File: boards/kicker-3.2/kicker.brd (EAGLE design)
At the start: 141 x 146.1 mm, 160 parts, among them J1 B2PS-VH(LF)(SN), J2 HFW8R-1ST, J3 B2PS-VH(LF)(SN), J4 B2PS-VH(LF)(SN), J5 2-PIN_2MM-H, J6 3-PIN_2MM-H, J7 !BTN_KCK_PRE_EXT, J8 !BTN_CHP_PRE_EXT, J9 !BTN_CHG_PRE_EXT, Q1 ATP302ATPAK, Q10 BSS806NSOT-23-3, Q2 IRFS4227, Q3 BSS127, Q4 BSS127, Q5 BSS127, Q6 BSS127, Q7 AOD1N60, T1 DA203X-ALDA2034, U1 MPM3620GQV-P, U2 15V, U3 LT3751FE, U4 AT32ATQFP44, U5 IX4427N, U6 MAX6817, U7 MAX6817

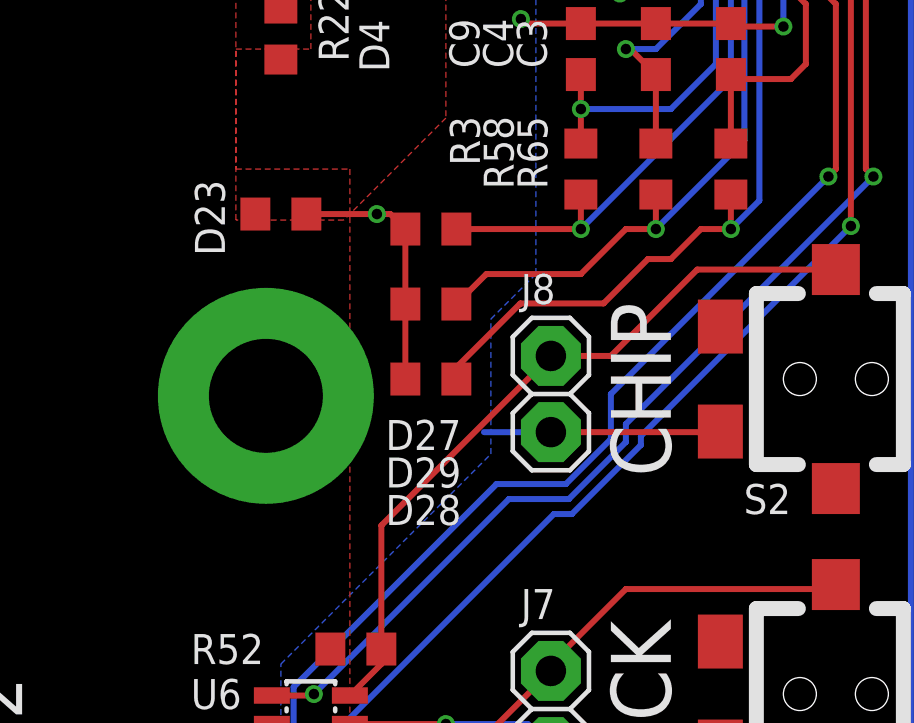
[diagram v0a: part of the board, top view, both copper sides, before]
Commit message: remove unnecessary TVS diodes clapming DIO rails
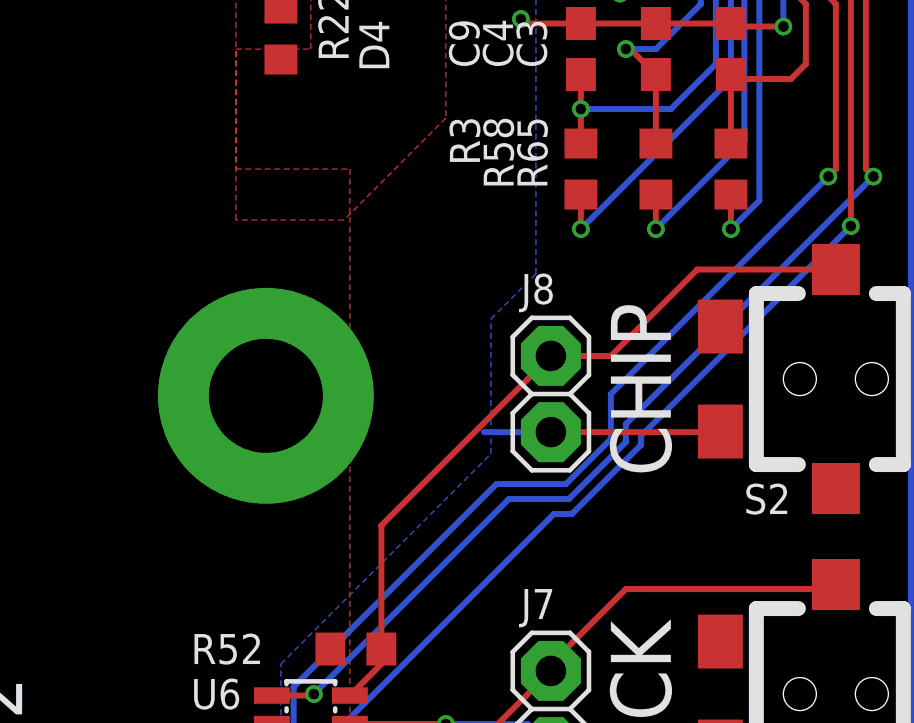
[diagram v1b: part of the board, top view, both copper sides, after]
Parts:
- removed D23, D27, D28, D29: PESD5V0C1USFYL, RoboJackets-Diodes:R0603
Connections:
- net !DONE!_RAW: no longer D29.2
- net !FAULT!_RAW: no longer D28.2
- net +5V: no longer D23.2
- net CHARGE_RAW: no longer D27.2
- net GND: no longer D23.1, D27.1, D28.1, D29.1
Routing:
- net !FAULT!_RAW: track 316.2 -> 304.7 mm
- net GND: track 355.0 -> 346.5 mm, vias 355 -> 354
- net !DONE!_RAW: track 304.3 -> 296.6 mm
- net CHARGE_RAW: track 292.3 -> 288.2 mm
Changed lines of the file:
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@@
 <attribute name="VALUE" x="-51.465" y="-16.295" size="1.27" layer="27" rot="R180"/>
-</element>
-<element name="D23" library="RoboJackets-Diodes" package="R0603" package3d_urn="urn:adsk.eagle:package:23555/3" value="PESD5V0C1USFYL" x="49" y="7" smashed="yes" rot="R180">
-<attribute name="NAME" x="46.135" y="8.135" size="1" layer="25" rot="R270"/>
-<attribute name="VALUE" x="49.635" y="8.905" size="1.27" layer="27" rot="R180"/>
 </element>
 <element name="D5" library="RoboJackets-LEDs" package="CHIP-LED0603" value="YELLOW" x="32.5" y="74.5" smashed="yes" rot="R180">
@@
 <attribute name="NAME" x="55.615" y="11.865" size="1" layer="25" font="vector" rot="R90"/>
 <attribute name="VALUE" x="60.905" y="11.865" size="1.27" layer="27" rot="R90"/>
-</element>
-<element name="D27" library="RoboJackets-Diodes" package="R0603" package3d_urn="urn:adsk.eagle:package:23555/3" value="PESD5V0C1USFYL" x="54" y="6.5" smashed="yes">
-<attribute name="NAME" x="52.49" y="-0.865" size="1" layer="25" font="vector"/>
-<attribute name="VALUE" x="53.365" y="4.595" size="1.27" layer="27"/>
-</element>
-<element name="D28" library="RoboJackets-Diodes" package="R0603" package3d_urn="urn:adsk.eagle:package:23555/3" value="PESD5V0C1USFYL" x="54" y="1.5" smashed="yes">
-<attribute name="NAME" x="52.49" y="-3.365" size="1" layer="25" font="vector"/>
-<attribute name="VALUE" x="53.365" y="-0.405" size="1.27" layer="27"/>
-</element>
-<element name="D29" library="RoboJackets-Diodes" package="R0603" package3d_urn="urn:adsk.eagle:package:23555/3" value="PESD5V0C1USFYL" x="54" y="4" smashed="yes">
-<attribute name="NAME" x="52.49" y="-2.115" size="1" layer="25" font="vector"/>
-<attribute name="VALUE" x="53.365" y="2.095" size="1.27" layer="27"/>
 </element>
 <element name="R4" library="rcl" package="R0603" value="100k" x="41" y="65.5" smashed="yes" rot="MR180">
@@
 <contactref element="U4" pad="28"/>
 <contactref element="U4" pad="39"/>
-<contactref element="D23" pad="1"/>
 <contactref element="C9" pad="2"/>
 <contactref element="R4" pad="1"/>
-<contactref element="D27" pad="1"/>
-<contactref element="D28" pad="1"/>
 <contactref element="C3" pad="2"/>
 <contactref element="C4" pad="2"/>
-<contactref element="D29" pad="1"/>
 <contactref element="C11" pad="-"/>
 <contactref element="C29" pad="2"/>
@@
 <wire x1="57.15" y1="13.35" x2="57" y2="13.5" width="0.2" layer="1"/>
 <via x="57" y="13.5" extent="1-16" drill="0.35"/>
-<wire x1="49.85" y1="7" x2="52.2" y2="7" width="0.2" layer="1"/>
-<via x="52.2" y="7" extent="1-16" drill="0.35"/>
-<wire x1="52.65" y1="7" x2="53.15" y2="6.5" width="0.2" layer="1"/>
-<wire x1="52.65" y1="7" x2="52.2" y2="7" width="0.2" layer="1"/>
-<wire x1="53.15" y1="6.5" x2="53.15" y2="4" width="0.2" layer="1"/>
-<wire x1="53.15" y1="4" x2="53.15" y2="1.5" width="0.2" layer="1"/>
 <via x="-37.25" y="1" extent="1-16" drill="0.35"/>
 <contactref element="D24" pad="A"/>
@@
 <wire x1="34.5" y1="71" x2="34.5" y2="69.5" width="0.1524" layer="1"/>
 <contactref element="C2" pad="1"/>
-<contactref element="D23" pad="2"/>
 <wire x1="47.45" y1="58.05" x2="47.45" y2="57.022878125" width="0.2" layer="1"/>
 <wire x1="34.5" y1="71" x2="47.45" y2="58.05" width="0.2" layer="1"/>
@@
 <contactref element="R3" pad="2"/>
 <contactref element="R4" pad="2"/>
-<contactref element="D27" pad="2"/>
 <wire x1="-69.1" y1="46.3" x2="-69.1" y2="-11.55" width="0.2" layer="16"/>
 <wire x1="-69.1" y1="46.3" x2="-63.475" y2="51.925" width="0.2" layer="16"/>
@@
 <wire x1="64" y1="27.025" x2="64" y2="11.5" width="0.2" layer="16"/>
 <wire x1="45.6" y1="65.5" x2="41.85" y2="65.5" width="0.2" layer="16"/>
-<wire x1="59" y1="6.5" x2="54.85" y2="6.5" width="0.2" layer="1"/>
 <wire x1="-7.2" y1="75.9" x2="-6.3556" y2="75.9" width="0.2" layer="16"/>
 <wire x1="-6.3556" y1="75.9" x2="-6.3506" y2="75.895" width="0.2" layer="16"/>
@@
 <contactref element="R19" pad="1"/>
 <contactref element="R58" pad="2"/>
-<contactref element="D29" pad="2"/>
 <wire x1="39.725" y1="67.75" x2="41.625" y2="67.75" width="0.2" layer="16"/>
 <via x="41.625" y="67.75" extent="1-16" drill="0.35"/>
@@
 <wire x1="46.375" y1="63" x2="46.5" y2="63" width="0.2" layer="1"/>
 <wire x1="46.375" y1="63" x2="41.625" y2="67.75" width="0.2" layer="1"/>
-<wire x1="61.5" y1="6.5" x2="60.5" y2="6.5" width="0.2" layer="1"/>
-<wire x1="60.5" y1="6.5" x2="59" y2="5" width="0.2" layer="1"/>
-<wire x1="59" y1="5" x2="55.85" y2="5" width="0.2" layer="1"/>
-<wire x1="55.85" y1="5" x2="54.85" y2="4" width="0.2" layer="1"/>
 <via x="-6" y="76.5" extent="1-16" drill="0.35"/>
 <wire x1="-7.175" y1="76.5" x2="-6" y2="76.5" width="0.2" layer="16"/>
@@
 <contactref element="U3" pad="6"/>
 <contactref element="R65" pad="2"/>
-<contactref element="D28" pad="2"/>
 <contactref element="R57" pad="1"/>
 <contactref element="Q4" pad="1"/>
@@
 <wire x1="41.5" y1="70" x2="47.5" y2="64" width="0.2" layer="1"/>
 <via x="47.5" y="64" extent="1-16" drill="0.35"/>
-<wire x1="64" y1="6.5" x2="63" y2="6.5" width="0.2" layer="1"/>
-<wire x1="63" y1="6.5" x2="62" y2="5.5" width="0.2" layer="1"/>
-<wire x1="62" y1="5.5" x2="61.235025" y2="5.5" width="0.2" layer="1"/>
-<wire x1="61.235025" y1="5.5" x2="59.755025" y2="4.02" width="0.2" layer="1"/>
-<wire x1="59.755025" y1="4.02" x2="56.98223125" y2="4.02" width="0.2" layer="1"/>
-<wire x1="56.98223125" y1="4.02" x2="54.85" y2="1.88776875" width="0.2" layer="1"/>
-<wire x1="54.85" y1="1.5" x2="54.85" y2="1.88776875" width="0.2" layer="1"/>
 <wire x1="-52.895" y1="62.605" x2="-52.895" y2="55.22249375" width="0.2" layer="16"/>
 <wire x1="-52.895" y1="55.22249375" x2="-55.26629375" y2="52.8512" width="0.2" layer="16"/>

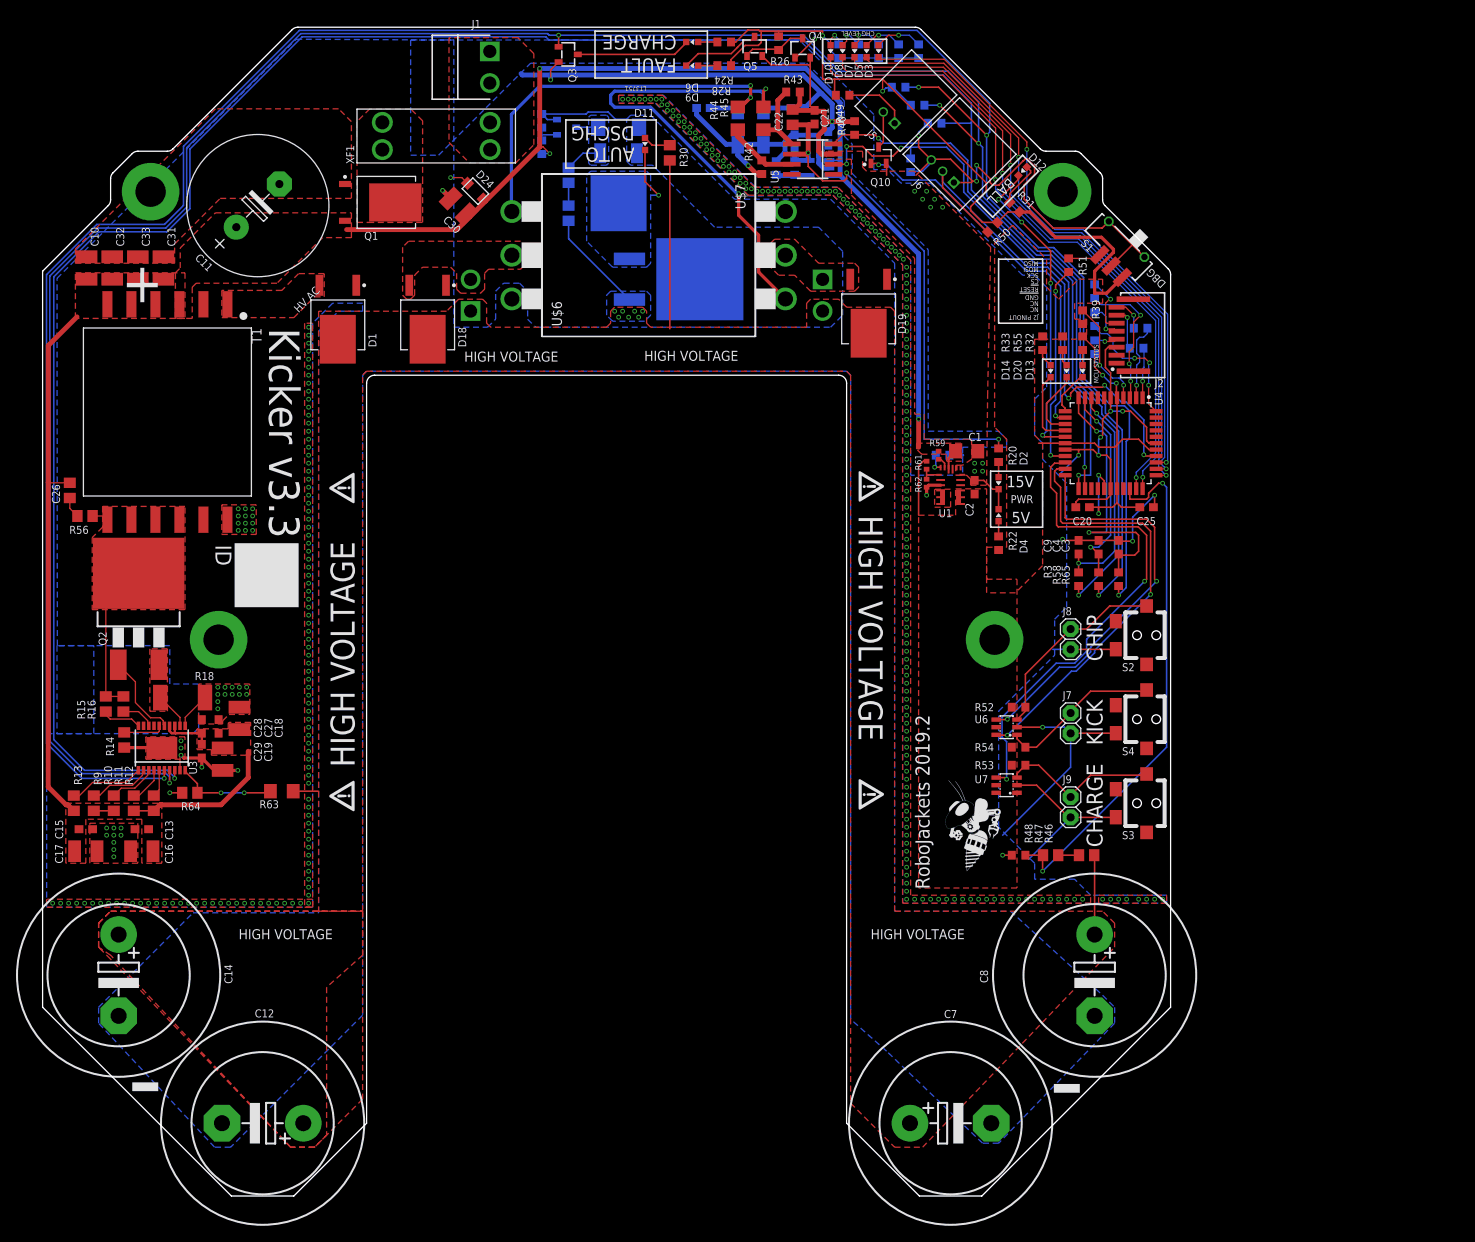
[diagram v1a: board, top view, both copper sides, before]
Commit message: kicker passing initial drc checks
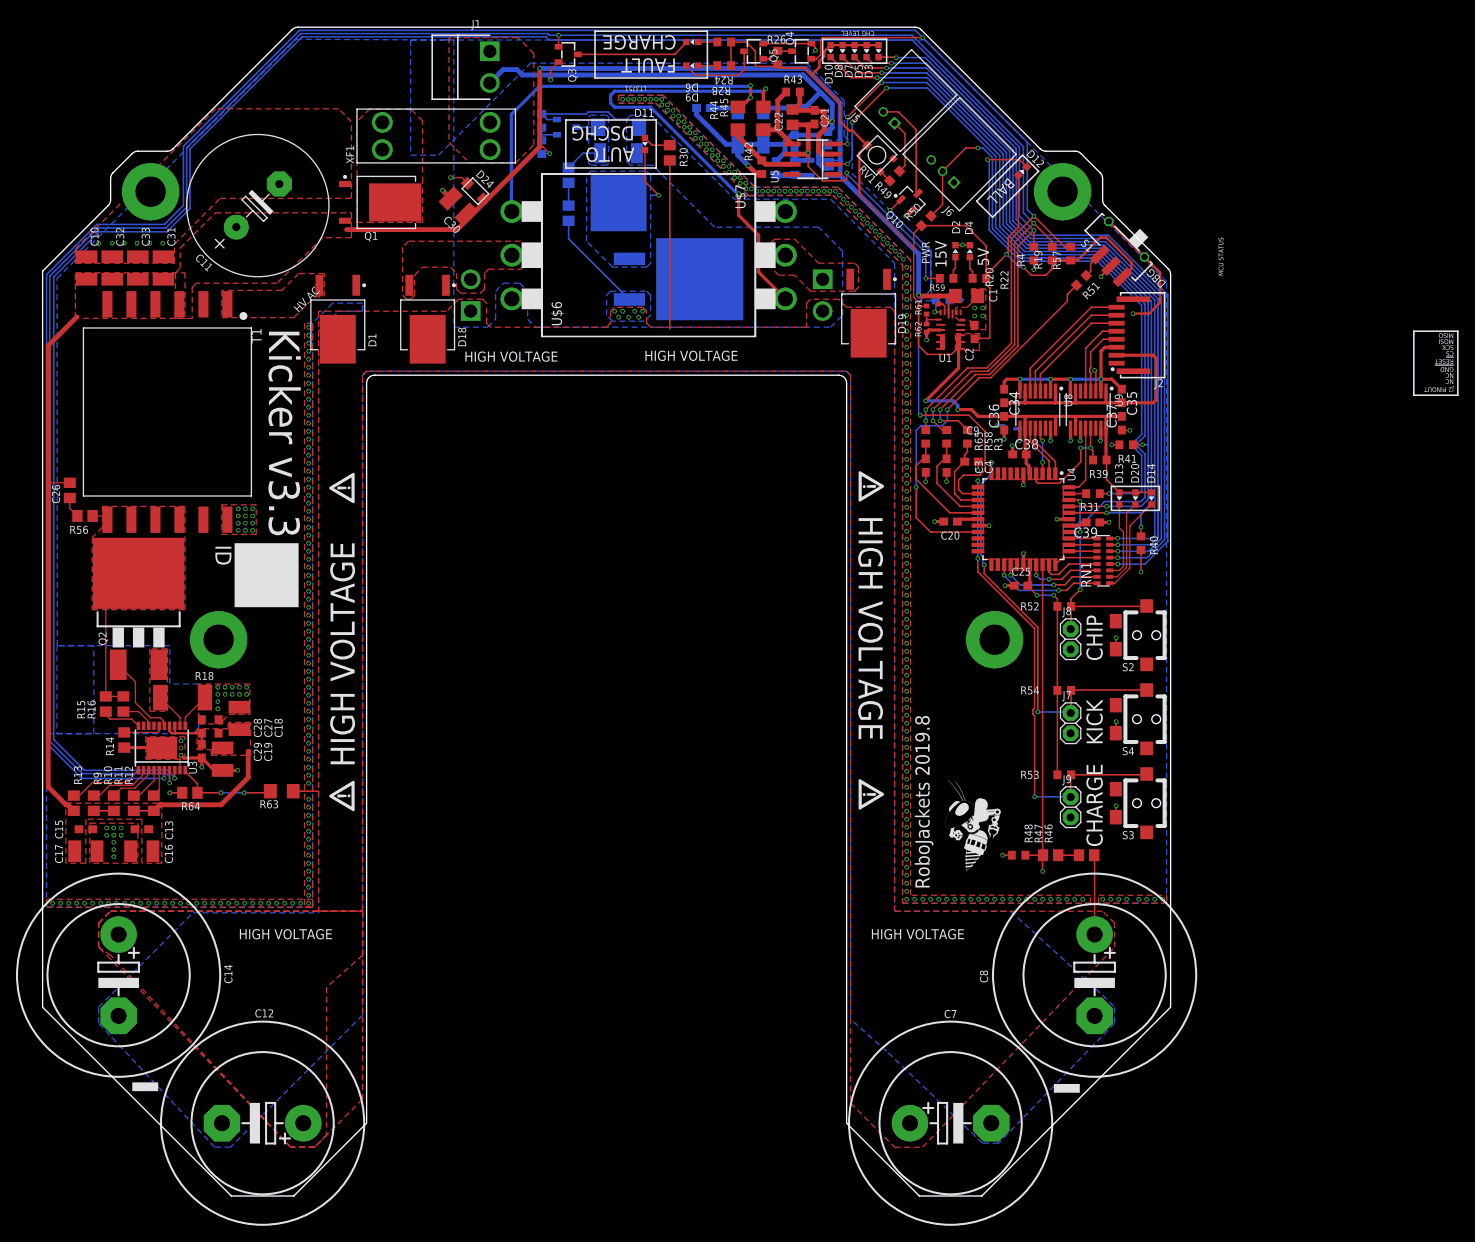
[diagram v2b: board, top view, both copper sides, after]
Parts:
- removed R21, R23, R32: 162, rcl:R0603
- removed R25, R27, R29, R33: 261, rcl:R0603
- removed R5, R6, R66, R7, R8: 2.7k, resistor:R0603
- removed R55: 60, rcl:R0603
- removed U6, U7: MAX6817, RoboJackets-ICs:SOT-23-6
- added C34, C35, C36, C37, C38, C39: 0.1uF, rcl:C0603
- added RN1: 330, RoboJackets-Resistors:RA-8_2506
- added RV1: 500, RoboJackets-Resistors:PVG3G
- added U8: ADUM744XCRQZ-RL7, RoboJackets-ICs:SOP63P574X165-16
- added U9: ADUM744XARQZ-RL7, RoboJackets-ICs:SOP63P574X165-16
- R22, R24: value 162 -> 330
- R28: value 261 -> 330
- moved R40 63.0 mm to (66.8, 13.0), turned to 90 degrees
- moved R41 44.1 mm to (65.0, 25.3), flipped to the top, turned to 0 degrees
- moved R31 37.1 mm to (60.8, 19.2), turned to 180 degrees
- moved D4 33.2 mm to (45.4, 49.5)
- moved R22 33.2 mm to (46.6, 46.1), turned to 0 degrees
- moved R65 30.0 mm to (39.9, 26.3), turned to 90 degrees
- moved R57 29.9 mm to (58.0, 49.2), flipped to the top, turned to 270 degrees
- moved D2 29.5 mm to (43.6, 49.5), turned to 0 degrees
- moved C3 26.2 mm to (39.9, 22.7), turned to 270 degrees
- moved R58 26.0 mm to (42.5, 26.3), turned to 90 degrees
- moved R19 25.0 mm to (55.7, 49.2), flipped to the top, turned to 270 degrees
- moved R20 23.0 mm to (42.5, 46.1), turned to 180 degrees
- moved R3 22.6 mm to (45.1, 26.3), turned to 90 degrees
- moved C4 21.6 mm to (42.5, 22.7), turned to 270 degrees
- moved R4 20.5 mm to (53.4, 49.2), flipped to the top, turned to 90 degrees
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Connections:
- removed net !BTN_CHG_PRE: J9.1, R53.1, S3.C, U7.3
- removed net !BTN_CHP_PRE: J8.1, R52.1, S2.C, U6.3
- removed net !BTN_KCK_PRE: J7.1, R54.1, S4.C, U6.1
- removed net !KICKER_SELECT_CL: J2.5, R8.1
- removed net !RESET_CL: J2.4, R66.1
- removed net MISO_CL: J2.8, R5.1
- removed net MOSI_CL: J2.7, R6.1
- removed net N$11: D3.A, R21.1
- removed net N$12: D5.A, R23.1
- removed net N$13: D7.A, R25.1
- removed net N$17: D20.A, R55.1
- removed net N$21: D8.A, R27.1
- removed net N$30: D10.A, R29.1
- removed net N$4: D13.A, R32.1
- removed net N$40: D12.A, R31.1
- removed net SCK_CL: J2.6, R7.1
- new net !KICKER_SELECT_EXT: J2.5, U9.5
- new net !RESET_EXT: J2.4, U9.4
- new net BALL_SENSE_CL: D12.C, R31.1
- new net GND_LGC_EXT: C34.1, C35.1, J2.3, U8.2, U8.8, U9.2, U9.8
- new net HV_IND_HIGH_CL: D8.C, RN1.7
- new net HV_IND_LOW_CL: D5.C, RN1.5
- new net HV_IND_MAX_CL: D10.C, RN1.8
- new net HV_IND_MID_CL: D7.C, RN1.6
- new net HV_IND_MIN_CL: D3.C, RN1.4
- new net MCU_ERR_CL: D14.C, RN1.1
- new net MCU_INIT_OK_CL: D13.C, RN1.3
- new net MCU_MODE_CL: D20.C, RN1.2
- new net MISO_EXT: J2.8, U8.6
- new net MOSI_EXT: J2.7, U8.5
- new net N$2: U8.3
- new net SCK_EXT: J2.6, U8.4
- new net VCC_LGC_EXT: C34.2, C35.2, J2.2, U8.1, U8.7, U9.1, U9.7
- net !BTN_CHG: now also J9.1, R53.1, S3.C, U4.12; no longer U4.20, U7.4
- net !BTN_CHP: now also J8.1, R52.1, S2.C, U4.42; no longer U4.22, U6.4
- net !BTN_KCK: now also J7.1, R54.1, S4.C, U4.11; no longer U4.21, U6.6
- net !DONE!: now also U4.15; no longer U4.10
- net !FAULT!: now also U4.16; no longer U4.11
- net !KICKER_SELECT: now also U9.12; no longer R8.2
- net !RESET: now also U9.13; no longer R66.2
- net +5V: now also C36.2, C37.2, C38.2, C39.2, D10.A, D12.A, D13.A, D14.A, D20.A, D3.A, D5.A, D7.A, D8.A, RV1.P$2, U8.10, U8.16, U9.10, U9.16; no longer R21.2, R23.2, R25.2, R27.2, R29.2, R31.2, R32.2, R33.2, R49.1, R55.2, U6.5, U7.5
- net BALL_SENSE: now also R31.2, U4.43; no longer D12.C, U4.16
- net CHARGE: now also U4.14; no longer U4.9
- net CHIP: now also U4.41; no longer U4.24
- net GND: now also C36.1, C37.1, C38.1, C39.1, U8.15, U8.9, U9.11, U9.15, U9.3, U9.9; no longer J2.3, U6.2, U7.2
- net HV_IND_HIGH: now also RN1.10, U4.35; no longer D8.C, U4.33
- net HV_IND_LOW: now also RN1.12, U4.33; no longer D5.C, U4.35
- net HV_IND_MAX: now also RN1.9, U4.36; no longer D10.C, U4.32
- net HV_IND_MID: now also RN1.11; no longer D7.C
- net HV_IND_MIN: now also RN1.13, U4.32; no longer D3.C, U4.36
- net KICK: now also U4.40; no longer U4.23
- net MCU_ERR: now also RN1.16, U4.25; no longer D14.C, U4.15
- net MCU_INIT_OK: now also RN1.14, U4.30; no longer D13.C, U4.12
- net MCU_MODE: now also RN1.15, U4.26; no longer D20.C, U4.14
- net MISO: now also U8.11; no longer R5.2
- net MOSI: now also U8.12; no longer R6.2
- net N$3: now also R49.1, RV1.P$3; no longer D14.A, R33.1
- net SCK: now also U8.13; no longer R7.2
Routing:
- net GND: track 346.5 -> 214.7 mm, vias 354 -> 373
- net HV_IND_MAX_CL: track 0.00 -> 93.5 mm, vias 0 -> 2
- net HV_IND_HIGH_CL: track 0.00 -> 93.4 mm, vias 0 -> 2
- net HV_IND_MID_CL: track 0.00 -> 93.2 mm, vias 0 -> 2
- net HV_IND_LOW_CL: track 0.00 -> 93.1 mm, vias 0 -> 2
- net HV_IND_MIN_CL: track 0.00 -> 92.9 mm, vias 0 -> 2
- net HV_IND_MAX: track 81.8 -> 3.52 mm, vias 2 -> 0
- net HV_IND_HIGH: track 80.2 -> 3.52 mm, vias 2 -> 0
- net HV_IND_MID: track 78.2 -> 3.52 mm, vias 2 -> 0
- net HV_IND_LOW: track 76.0 -> 5.57 mm, vias 2 -> 0
- net BALL_SENSE_CL: track 0.00 -> 66.4 mm, vias 0 -> 2
- net HV_IND_MIN: track 73.8 -> 7.58 mm, vias 2 -> 0
- net +5V: track 169.9 -> 231.1 mm
- net BALL_SENSE: track 39.5 -> 2.17 mm, vias 4 -> 0
- net VCC_LGC_EXT: track 0.00 -> 35.4 mm
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- removed copper zone on layer 1, net REG-SW
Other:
- board text added: "RoboJackets 2019.8"
- board text removed: "+"
- board text removed: "RoboJackets 2019.2"
